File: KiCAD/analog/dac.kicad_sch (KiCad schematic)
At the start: 15 parts, among them J11 Screw_Terminal_01x02, Q11 2N3904, Q12 2N3904, U4 MCP4922-EP

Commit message: KiCad revC: 15 missing footprints assigned + T68->T50 inductor swap
Fifteen components across the LPF and DAC Control sheets had empty
Footprint fields.  Assigned appropriate footprints matching project
conventions already used by equivalent parts:

LPF sheet (12):
  C9 100nF  -> Capacitor_THT:C_Disc_D5.0mm_W2.5mm_P5.00mm
  C10 10nF -> Capacitor_THT:C_Disc_D6.0mm_W2.5mm_P5.00mm
  R11 1K   -> Resistor_THT:R_Axial_DIN0207_L6.3mm_D2.5mm_P10.16mm_Horizontal
  J16, J25, J26, J27 (relay coil screw terminals)
           -> TerminalBlock_Phoenix:TerminalBlock_Phoenix_MKDS-1,5-2_1x02_P5.00mm_Horizontal
  TP7, TP10M1, TP15M1, TP17M1, TP20M1 (test points)
           -> Connector_PinHeader_2.54mm:PinHeader_1x01_P2.54mm_Vertical

DAC Control sheet (3):
  R10 10K  -> same resistor footprint as above
  J11      -> same Phoenix screw-terminal footprint as above
  U4 MCP4922-EP -> Package_DIP:DIP-14_W7.62mm (PDIP, consistent with
                   the LM7171 PDIP-8 footprints already in use)

Also in this commit:
  - Nine inductor footprints swapped from T68-6 to T50-6 variants
    (L7, L10, L11, L12, L13, L14, L15, L16, L17 -- the 17m, 15m, 10m
    LPF inductors; L4, L6, L9 were already T50-6).  Correctly reflects
    that all four LPFs now use T50-6 cores.
  - Netlist regenerated by user to pick up the TP band-ID symbols
    (TP20M1, TP17M1, TP15M1, TP10M1) and the footprint changes.

Co-Authored-By: Claude Opus 4.7 <noreply@anthropic.com>
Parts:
- J11: footprint (none) -> TerminalBlock_Phoenix:TerminalBlock_Phoenix_MKDS-1,5-2_1x02_P5.00mm_Horizontal
- R10: footprint (none) -> Resistor_THT:R_Axial_DIN0207_L6.3mm_D2.5mm_P10.16mm_Horizontal
- U4: footprint (none) -> Package_DIP:DIP-14_W7.62mm
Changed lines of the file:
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@@
 			)
 		)
-		(property "Footprint" ""
+		(property "Footprint" "TerminalBlock_Phoenix:TerminalBlock_Phoenix_MKDS-1,5-2_1x02_P5.00mm_Horizontal"
 			(at 161.29 46.99 0)
 			(hide yes)
@@
 			)
 		)
-		(property "Footprint" ""
+		(property "Footprint" "Package_DIP:DIP-14_W7.62mm"
 			(at 107.95 73.66 0)
 			(hide yes)
@@
 			)
 		)
-		(property "Footprint" ""
+		(property "Footprint" "Resistor_THT:R_Axial_DIN0207_L6.3mm_D2.5mm_P10.16mm_Horizontal"
 			(at 94.996 82.804 90)
 			(hide yes)

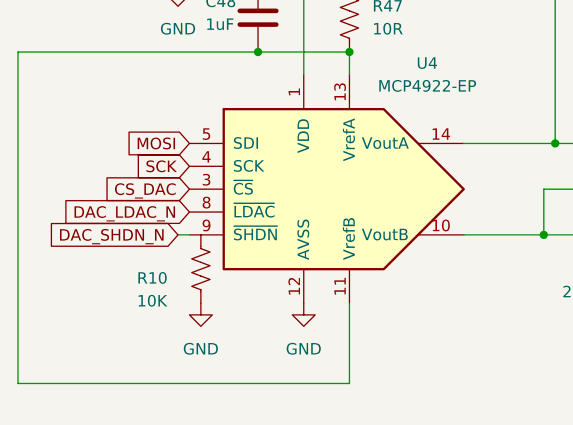
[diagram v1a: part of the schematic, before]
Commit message: KiCad revC: LM2940CT-5.0 symbol + ±12V subsystem migrated into analog/power
* xmitter.kicad_sym: new LM2940CT-5.0 symbol, pin-compat with 7805 (same
  TO-220 topology as the LM2940CT-12 added last commit). For the +5V rail
  feeding the Metro.

* analog/power.kicad_sch: substantial migration of the validated ±12V
  subsystem (LT1054 regulated inverter + LM2940CT-12 LDO) from the
  standalone KiCAD/power/ project.  Tube-era regulators (LM317L, LM7812,
  original LT1054 attempt) and bridge rectifier gone. Values still need
  final cleanup (R14=10K->20K, R15 string->240K, C16=1n->2.2n, C12 no
  value) before next sim validation.

* Not pushing yet — 28V relay doubler stage will land in the same sheet
  before this gets published.

Co-Authored-By: Claude Opus 4.7 <noreply@anthropic.com>
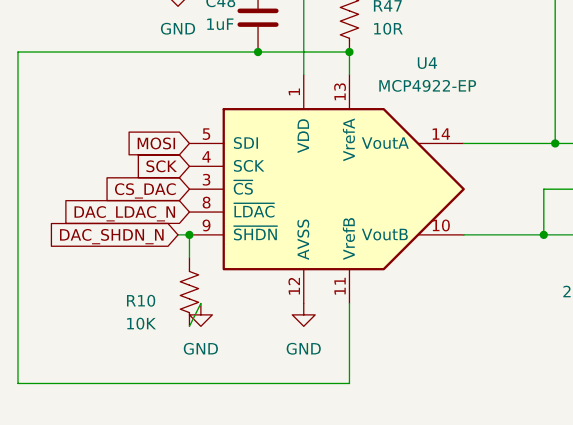
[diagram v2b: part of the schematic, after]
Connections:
- net DAC_SHDN_N: now also R10.1
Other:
- moved on the sheet: R10
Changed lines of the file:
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@@
+	)
+	(junction
+		(at 92.71 78.74)
+		(diameter 0)
+		(color 0 0 0 0)
 	)
 	(junction
@@
 	(wire
 		(pts
+			(xy 92.71 78.74) (xy 92.71 81.28)
+		)
+		(stroke
+			(width 0)
+			(type default)
+		)
+	)
+	(wire
+		(pts
 			(xy 73.66 58.42) (xy 100.33 58.42)
+		)
+		(stroke
+			(width 0)
+			(type default)
+		)
+	)
+	(wire
+		(pts
+			(xy 92.71 88.9) (xy 93.98 86.36)
 		)
 		(stroke
@@
 	(symbol
 		(lib_id "Device:R_US")
-		(at 93.98 82.55 0)
+		(at 92.71 85.09 0)
 		(unit 1)
 		(body_style 1)
@@
 		(dnp no)
 		(property "Reference" "R10"
-			(at 86.868 83.566 0)
+			(at 85.598 86.106 0)
 			(show_name no)
 			(do_not_autoplace no)
@@
 		)
 		(property "Value" "10K"
-			(at 86.868 86.106 0)
+			(at 85.598 88.646 0)
 			(show_name no)
 			(do_not_autoplace no)
@@
 		)
 		(property "Footprint" "Resistor_THT:R_Axial_DIN0207_L6.3mm_D2.5mm_P10.16mm_Horizontal"
-			(at 94.996 82.804 90)
+			(at 93.726 85.344 90)
 			(hide yes)
 			(show_name no)
@@
 		)
 		(property "Datasheet" ""
-			(at 93.98 82.55 0)
+			(at 92.71 85.09 0)
 			(hide yes)
 			(show_name no)
@@
 		)
 		(property "Description" "Resistor, US symbol"
-			(at 93.98 82.55 0)
-			(hide yes)
-			(show_name no)
+			(at 92.71 85.09 0)
+			(hide yes)
+			(show_name no)

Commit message: KiCad revC: resolve project-audit findings on analog + protoshield
Fixes the four items from Documentation/2026-10-11-project-audit.md
plus the follow-up Q11 series-R finding:

- Rename FAULT -> FAULT_N on analog arduino and protoshield to match
  ss_pa (active-low per the latest design spec in ss_pa.md)
- Delete the stale PA_OUTPUT_LEVEL global label on dac sheet
  (tube-era signal, no consumer; MCP4922 VoutA now unused and output
  connector marked DNP)
- Fix ENC_INT_CLEAN -> R6 -> ENC_INT signal path on analog arduino
  so the encoder interrupt actually reaches the Metro via protoshield
- Re-export analog.net so it reflects the current schematic (J31
  RJ45 to ss_pa, bias/sense/fault signals, R6 wiring, etc.)

Co-Authored-By: Claude Opus 4.7 <noreply@anthropic.com>
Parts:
- added R13: 1K, symbol Device:R_US
- J11: now not fitted
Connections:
- net Gate 2: now also R13.2; no longer U4.10 (VoutB)
- net PA_OUTPUT_LEVEL: no longer names the net of J11.2 (Pin_2), U4.14 (VoutA)
- new net: R13.1, U4.10 (VoutB)
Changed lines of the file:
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@@
-	)
-	(junction
-		(at 133.35 68.58)
-		(diameter 0)
-		(color 0 0 0 0)
 	)
 	(junction
@@
 	(wire
 		(pts
-			(xy 138.43 68.58) (xy 133.35 68.58)
-		)
-		(stroke
-			(width 0)
-			(type default)
-		)
-	)
-	(wire
-		(pts
 			(xy 133.35 68.58) (xy 123.19 68.58)
 		)
@@
 	(wire
 		(pts
-			(xy 92.71 88.9) (xy 93.98 86.36)
+			(xy 92.71 88.9) (xy 92.71 90.17)
 		)
 		(stroke
@@
 	(wire
 		(pts
-			(xy 123.19 78.74) (xy 132.08 78.74)
+			(xy 123.19 78.74) (xy 124.46 78.74)
 		)
 		(stroke
@@
 		(property "Intersheetrefs" "${INTERSHEET_REFS}"
 			(at 186.5909 78.74 0)
-			(hide yes)
-			(show_name no)
-			(do_not_autoplace no)
-			(effects
-				(font
-					(size 1.27 1.27)
-				)
-				(justify left)
-			)
-		)
-	)
-	(global_label "PA_OUTPUT_LEVEL"
-		(shape output)
-		(at 138.43 68.58 0)
-		(fields_autoplaced yes)
-		(effects
-			(font
-				(size 1.27 1.27)
-			)
-			(justify left)
-		)
-		(property "Intersheetrefs" "${INTERSHEET_REFS}"
-			(at 158.3485 68.58 0)
 			(hide yes)
 			(show_name no)
@@
 		(on_board yes)
 		(in_pos_files yes)
-		(dnp no)
+		(dnp yes)
 		(property "Reference" "J11"
 			(at 163.83 46.9901 0)
@@
 	(symbol
 		(lib_id "power:GND")
-		(at 93.98 86.36 0)
+		(at 92.71 90.17 0)
 		(unit 1)
 		(body_style 1)
@@
 		(fields_autoplaced yes)
 		(property "Reference" "#PWR039"
-			(at 93.98 92.71 0)
+			(at 92.71 96.52 0)
 			(hide yes)
 			(show_name no)
@@
 		)
 		(property "Value" "GND"
-			(at 93.98 91.44 0)
+			(at 92.71 95.25 0)
 			(show_name no)
 			(do_not_autoplace no)
@@
 		)
 		(property "Footprint" ""
-			(at 93.98 86.36 0)
+			(at 92.71 90.17 0)
 			(hide yes)
 			(show_name no)
@@
 		)
 		(property "Datasheet" ""
-			(at 93.98 86.36 0)
+			(at 92.71 90.17 0)
 			(hide yes)
 			(show_name no)
@@
 		)
 		(property "Description" "Power symbol creates a global label with name \"GND\" , ground"
-			(at 93.98 86.36 0)
+			(at 92.71 90.17 0)
 			(hide yes)
 			(show_name no)
@@
 					(unit 1)
 				)
+			)
+		)
+	)
+	(symbol
+		(lib_id "Device:R_US")
+		(at 128.27 78.74 90)
+		(unit 1)
+		(body_style 1)
+		(exclude_from_sim no)
+		(in_bom yes)
+		(on_board yes)
+		(in_pos_files yes)
+		(dnp no)
+		(fields_autoplaced yes)
+		(property "Reference" "R13"
+			(at 128.27 72.39 90)
+			(show_name no)
+			(do_not_autoplace no)
+			(effects
+				(font
+					(size 1.27 1.27)
+				)
+			)
+		)
+		(property "Value" "1K"
+			(at 128.27 74.93 90)
+			(show_name no)
+			(do_not_autoplace no)
+			(effects
+				(font
+					(size 1.27 1.27)
+				)
+			)
+		)
+		(property "Footprint" ""
+			(at 128.524 77.724 90)
+			(hide yes)
+			(show_name no)
+			(do_not_autoplace no)
+			(effects
+				(font
+					(size 1.27 1.27)
+				)
+			)
+		)
+		(property "Datasheet" ""
+			(at 128.27 78.74 0)
+			(hide yes)
+			(show_name no)
+			(do_not_autoplace no)
+			(effects
+				(font
+					(size 1.27 1.27)
+				)
+			)
+		)
+		(property "Description" "Resistor, US symbol"
+			(at 128.27 78.74 0)
+			(hide yes)
+			(show_name no)
+			(do_not_autoplace no)
+			(effects
+				(font
+					(size 1.27 1.27)
+				)
+			)
+		)
+		(pin "1"
+		)
+		(pin "2"
+		)
+		(instances
+			(project "analog"
+				(path "/d3de40b8-856b-4fbd-829c-f45ffcd55742/e880f7dd-82a1-4efe-84f5-e6a9d5641736"
+					(reference "R13")
+					(unit 1)
+				)

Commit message: revC: accumulated schematic/netlist updates + BOM tooling
- analog + ss_pa netlists regenerated to current schematic state
- interface/arduino/dac/power sheet updates on analog
- fault_shutdown and pa_stage edits on ss_pa (footprint assignments)
- assign_cap_footprints.py: additional VALUE_TO_FOOTPRINT entries
- gen_board_boms.py: per-board BOM generator (multi-sheet .xlsx by
  component category, first-match-wins bucketing, DNP exclusion)
- gen_total_bom.py: consolidated BOM across analog + frontpanel + ss_pa
  for a single Mouser order, board-prefixed references, mixed-footprint
  flagging per Value row

Co-Authored-By: Claude Opus 4.7 <noreply@anthropic.com>
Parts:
- R13: footprint (none) -> Resistor_THT:R_Axial_DIN0207_L6.3mm_D2.5mm_P10.16mm_Horizontal
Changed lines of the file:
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@@
 			)
 		)
-		(property "Footprint" ""
+		(property "Footprint" "Resistor_THT:R_Axial_DIN0207_L6.3mm_D2.5mm_P10.16mm_Horizontal"
 			(at 128.524 77.724 90)
 			(hide yes)

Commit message: revD: DGFET-DAC bias scheme, kit-style xfmr naming, custom footprints, Output LPF project
Architecture refinements since the previous revD commit (f8d7058):

Analog board (vfo_complete, arduino, dac, power sheets):
  * MCP4922 (U4) ch B exposed as DRIVER_BIAS DAC output -> J31 pin 6
    (replaces the +3.3V pin that was on J31 pin 6 before). Analog's U4
    now controls the ss_pa BS170 driver DC bias point directly from
    firmware -- cleaner than the kit's trimmer+Q201 scheme.
  * MCP4728 (U3) ch A/B exposed as PA_Bias_A_Raw / PA_Bias_B_Raw ->
    J31 pins 7, 8. These feed the ss_pa CD74HC4066 fault-switch (U2),
    which gates them to PA_Bias_A/B on the IRF510 gates. On FAULT_N
    low, switch opens -> IRF510 bias collapses -> conduction cuts.
  * Rename pass: Bias_A/B/_Raw labels -> PA_Bias_A/B/_Raw everywhere
    (analog J3 screw-terminal, umbilical J31, ss_pa U2 inputs). Prefix
    disambiguates from DRIVER_BIAS which drives a different stage.
  * J2 (band-select RJ45 to Output LPF board): added RLY_40 provision.
    Pin layout reorganized -- RLY_40 lives at pin 5, pin 6 kept as a
    spare for a future 6th band.

ss_pa board (pa_stage, fault_shutdown, lpf sheets):
  * Driver + final BS170/IRF510 topology drawn following QRP Labs
    10W Linear kit (RF IN -> T201 input xfmr -> BS170 PP driver
    (Q2, Q6) -> T202 interstage -> IRF510 PP finals (Q3, Q4) ->
    T203 bifilar drain feed -> T204 output xfmr -> RF out).
  * Transformer references renamed to match the kit: T201 (input,
    BN61-2402), T202 (interstage, BN61-2402), T203 (drain feed,
    T50-43), T204 (output, BN43-202).
  * Driver bias filter on DRIVER_BIAS: C19 (0.1uF) + C20 (100pF)
    bulk + HF bypass, into T201 secondary CT (pin 4).
  * +3.3V now locally regulated on ss_pa (MCP1700x-330xxTO, U13)
    from +13.8V, powering U1 (LM393) and U2 (CD74HC4066). J31
    pin 6 freed up for DRIVER_BIAS.
  * Duplicate RJ45 J7 deleted (was a leftover from pre-DAC-bias era).
  * J3 (SMA RF input from analog) foo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
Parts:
- removed J11: Screw_Terminal_01x02, TerminalBlock_Phoenix:TerminalBlock_Phoenix_MKDS-1,5-2_1x02_P5.00mm_Horizontal, symbol Connector:Screw_Terminal_01x02
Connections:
- net DRIVER_BIAS: now reaches U4.14 (VoutA)
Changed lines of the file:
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@@
-	(wire
-		(pts
-			(xy 156.21 44.45) (xy 133.35 44.45)
-		)
-		(stroke
-			(width 0)
-			(type default)
-		)
-	)
 	(wire
 		(pts
@@
 		(pts
 			(xy 110.49 48.26) (xy 110.49 50.8)
-		)
-		(stroke
-			(width 0)
-			(type default)
-		)
-	)
-	(wire
-		(pts
-			(xy 133.35 44.45) (xy 133.35 68.58)
 		)
 		(stroke
@@
 				)
 				(justify right)
+			)
+		)
+	)
+	(global_label "DRIVER_BIAS"
+		(shape output)
+		(at 133.35 68.58 0)
+		(fields_autoplaced yes)
+		(effects
+			(font
+				(size 1.27 1.27)
+			)
+			(justify left)
+		)
+		(property "Intersheetrefs" "${INTERSHEET_REFS}"
+			(at 148.1281 68.58 0)
+			(hide yes)
+			(show_name no)
+			(do_not_autoplace no)
+			(effects
+				(font
+					(size 1.27 1.27)
+				)
+				(justify left)
 			)
 		)
@@
 				(path "/d3de40b8-856b-4fbd-829c-f45ffcd55742/e880f7dd-82a1-4efe-84f5-e6a9d5641736"
 					(reference "C48")
-					(unit 1)
-				)
-			)
-		)
-	)
-	(symbol
-		(lib_id "Connector:Screw_Terminal_01x02")
-		(at 161.29 46.99 0)
-		(mirror x)
-		(unit 1)
-		(body_style 1)
-		(exclude_from_sim no)
-		(in_bom yes)
-		(on_board yes)
-		(in_pos_files yes)
-		(dnp yes)
-		(property "Reference" "J11"
-			(at 163.83 46.9901 0)
-			(show_name no)
-			(do_not_autoplace no)
-			(effects
-				(font
-					(size 1.27 1.27)
-				)
-				(justify left)
-			)
-		)
-		(property "Value" "Screw_Terminal_01x02"
-			(at 163.83 44.4501 0)
-			(show_name no)
-			(do_not_autoplace no)
-			(effects
-				(font
-					(size 1.27 1.27)
-				)
-				(justify left)
-			)
-		)
-		(property "Footprint" "TerminalBlock_Phoenix:TerminalBlock_Phoenix_MKDS-1,5-2_1x02_P5.00mm_Horizontal"
-			(at 161.29 46.99 0)
-			(hide yes)
-			(show_name no)
-			(do_not_autoplace no)
-			(effects
-				(font
-					(size 1.27 1.27)
-				)
-			)
-		)
-		(property "Datasheet" ""
-			(at 161.29 46.99 0)
-			(hide yes)
-			(show_name no)
-			(do_not_autoplace no)
-			(effects
-				(font
-					(size 1.27 1.27)
-				)
-			)
-		)
-		(property "Description" "Generic screw terminal, single row, 01x02, script generated (kicad-library-utils/schlib/autogen/connector/)"
-			(at 161.29 46.99 0)
-			(hide yes)
-			(show_name no)
-			(do_not_autoplace no)
-			(effects
-				(font
-					(size 1.27 1.27)
-				)
-			)
-		)
-		(pin "1"
-		)
-		(pin "2"
-		)
-		(instances
-			(project "analog"
-				(path "/d3de40b8-856b-4fbd-829c-f45ffcd55742/e880f7dd-82a1-4efe-84f5-e6a9d5641736"
-					(reference "J11")
 					(unit 1)
 				)
@@
 					(unit 1)
 				)
-			)
-		)
-	)
-	(symbol
-		(lib_id "power:GND")
-		(at 156.21 46.99 0)
-		(unit 1)
-		(body_style 1)
-		(exclude_from_sim no)
-		(in_bom yes)
-		(on_board yes)
-		(in_pos_files yes)
-		(dnp no)
-		(fields_autoplaced yes)
-		(property "Reference" "#PWR027"
-			(at 156.21 53.34 0)
-			(hide yes)
-			(show_name no)
-			(do_not_autoplace no)
-			(effects
-				(font
-					(size 1.27 1.27)
-				)
-			)
-		)
-		(property "Value" "GND"
-			(at 156.21 52.07 0)
-			(show_name no)
-			(do_not_autoplace no)
-			(effects
-				(font
-					(size 1.27 1.27)
-				)
-			)
-		)
-		(property "Footprint" ""
-			(at 156.21 46.99 0)
-			(hide yes)
-			(show_name no)
-			(do_not_autoplace no)
-			(effects
-				(font
-					(size 1.27 1.27)
-				)
-			)
-		)
-		(property "Datasheet" ""
-			(at 156.21 46.99 0)
-			(hide yes)
-			(show_name no)
-			(do_not_autoplace no)
-			(effects
-				(font
-					(size 1.27 1.27)
-				)
-			)
-		)
-		(property "Description" "Power symbol creates a global label with name \"GND\" , ground"
-			(at 156.21 46.99 0)
-			(hide yes)
-			(show_name no)
-			(do_not_autoplace no)
-			(effects
-				(font
-					(size 1.27 1.27)
-				)
-			)
-		)
-		(pin "1"
-		)
-		(instances
-			(project "analog"
-				(path "/d3de40b8-856b-4fbd-829c-f45ffcd55742/e880f7dd-82a1-4efe-84f5-e6a9d5641736"
-					(reference "#PWR027")
-					(unit 1)
-				)

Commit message: revD analog: J23/J24 SMAs removed, many test points added, test_points.md
Schematic cleanup round:
  * Deleted J23 and J24 (SMAs that had carried GRID_CTL_A/B).
    These were redundant now that J35 is the production tube-PA
    control umbilical. Bench probing of GRID_CTL_A/B is now via
    TP2/TP1 (test-point pads) instead of SMA jacks.
  * Added 21 test points (TP1..TP21) across arduino, dac, and
    vfo_complete sheets. Covers:
      - Tube-PA control bus (TP1,2,5,6,7)
      - SS PA bias/sense/fault (TP3,4,12,13,14,15)
      - Keyer / envelope / U1 output (TP10,20,21)
      - DAC control lines (TP8,9)
      - Relay driver gates (TP11,16,17,18)
      - Hardware watchdog trigger (TP19)
    All on standard test-point pads for scope-probe or DMM access.

New doc: Documentation/test_points.md
  * Grouped TP table by functional area
  * Includes source/description for each signal
  * Includes a "how to use at the bench" section with common
    debug workflows (RF chain, bias setting, fault chain,
    future tube-PA bring-up, watchdog verification)
  * Uses monospace-aligned columns rather than markdown tables,
    per project convention for saved docs

Co-Authored-By: Claude Opus 4.7 <noreply@anthropic.com>
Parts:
- added TP15, TP20: xTP, Connector_PinHeader_2.54mm:PinHeader_1x01_P2.54mm_Vertical, symbol xmitter:xTP
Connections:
- net DRIVER_BIAS: now also TP15.1
- net Gate 2: now also TP20.1
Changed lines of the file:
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@@
+	)
+	(junction
+		(at 128.27 68.58)
+		(diameter 0)
+		(color 0 0 0 0)
 	)
 	(junction
@@
 	(wire
 		(pts
-			(xy 133.35 68.58) (xy 123.19 68.58)
+			(xy 133.35 68.58) (xy 128.27 68.58)
 		)
 		(stroke
@@
 	(wire
 		(pts
+			(xy 132.08 78.74) (xy 132.08 87.63)
+		)
+		(stroke
+			(width 0)
+			(type default)
+		)
+	)
+	(wire
+		(pts
 			(xy 105.41 50.8) (xy 110.49 50.8)
 		)
@@
 		(pts
 			(xy 176.53 63.5) (xy 185.42 63.5)
+		)
+		(stroke
+			(width 0)
+			(type default)
+		)
+	)
+	(wire
+		(pts
+			(xy 128.27 68.58) (xy 123.19 68.58)
 		)
 		(stroke
@@
 	)
 	(symbol
+		(lib_id "xmitter:xTP")
+		(at 132.08 87.63 180)
+		(unit 1)
+		(body_style 1)
+		(exclude_from_sim no)
+		(in_bom yes)
+		(on_board yes)
+		(in_pos_files yes)
+		(dnp no)
+		(fields_autoplaced yes)
+		(property "Reference" "TP20"
+			(at 134.62 89.6619 0)
+			(show_name no)
+			(do_not_autoplace no)
+			(effects
+				(font
+					(size 1.27 1.27)
+				)
+				(justify right)
+			)
+		)
+		(property "Value" "xTP"
+			(at 134.62 92.2019 0)
+			(show_name no)
+			(do_not_autoplace no)
+			(effects
+				(font
+					(size 1.27 1.27)
+				)
+				(justify right)
+			)
+		)
+		(property "Footprint" "Connector_PinHeader_2.54mm:PinHeader_1x01_P2.54mm_Vertical"
+			(at 127 87.63 0)
+			(hide yes)
+			(show_name no)
+			(do_not_autoplace no)
+			(effects
+				(font
+					(size 1.27 1.27)
+				)
+			)
+		)
+		(property "Datasheet" ""
+			(at 127 87.63 0)
+			(hide yes)
+			(show_name no)
+			(do_not_autoplace no)
+			(effects
+				(font
+					(size 1.27 1.27)
+				)
+			)
+		)
+		(property "Description" "xmitter project test point on broken-off 0.1 inch square pin header; put signal name in Value field so it becomes silk on the PCB"
+			(at 132.08 87.63 0)
+			(hide yes)
+			(show_name no)
+			(do_not_autoplace no)
+			(effects
+				(font
+					(size 1.27 1.27)
+				)
+			)
+		)
+		(pin "1"
+		)
+		(instances
+			(project "analog"
+				(path "/d3de40b8-856b-4fbd-829c-f45ffcd55742/e880f7dd-82a1-4efe-84f5-e6a9d5641736"
+					(reference "TP20")
+					(unit 1)
+				)
+			)
+		)
+	)
+	(symbol
 		(lib_id "Device:R_US")
 		(at 110.49 54.61 0)
@@
 					(unit 1)
 				)
+			)
+		)
+	)
+	(symbol
+		(lib_id "xmitter:xTP")
+		(at 128.27 68.58 0)
+		(unit 1)
+		(body_style 1)
+		(exclude_from_sim no)
+		(in_bom yes)
+		(on_board yes)
+		(in_pos_files yes)
+		(dnp no)
+		(fields_autoplaced yes)
+		(property "Reference" "TP15"
+			(at 130.81 64.0079 0)
+			(show_name no)
+			(do_not_autoplace no)
+			(effects
+				(font
+					(size 1.27 1.27)
+				)
+				(justify left)
+			)
+		)
+		(property "Value" "xTP"
+			(at 130.81 66.5479 0)
+			(show_name no)
+			(do_not_autoplace no)
+			(effects
+				(font
+					(size 1.27 1.27)
+				)
+				(justify left)
+			)
+		)
+		(property "Footprint" "Connector_PinHeader_2.54mm:PinHeader_1x01_P2.54mm_Vertical"
+			(at 133.35 68.58 0)
+			(hide yes)
+			(show_name no)
+			(do_not_autoplace no)
+			(effects
+				(font
+					(size 1.27 1.27)
+				)
+			)
+		)
+		(property "Datasheet" ""
+			(at 133.35 68.58 0)
+			(hide yes)
+			(show_name no)
+			(do_not_autoplace no)
+			(effects
+				(font
+					(size 1.27 1.27)
+				)
+			)
+		)
+		(property "Description" "xmitter project test point on broken-off 0.1 inch square pin header; put signal name in Value field so it becomes silk on the PCB"
+			(at 128.27 68.58 0)
+			(hide yes)
+			(show_name no)
+			(do_not_autoplace no)
+			(effects
+				(font
+					(size 1.27 1.27)
+				)
+			)
+		)
+		(pin "1"
+		)
+		(instances
+			(project "analog"
+				(path "/d3de40b8-856b-4fbd-829c-f45ffcd55742/e880f7dd-82a1-4efe-84f5-e6a9d5641736"
+					(reference "TP15")
+					(unit 1)
+				)
